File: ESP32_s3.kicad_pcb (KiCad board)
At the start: 2 copper layers, 100 x 80 mm, 67 parts, among them J1 54-00127, J11 backup, J14 TXRX, J15 TXRX2, J3 Conn_01x02, J4 Servo motor, J6 jetson nano, J7 Conn_01x02, J8 Conn_01x02, J9 Conn_01x02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

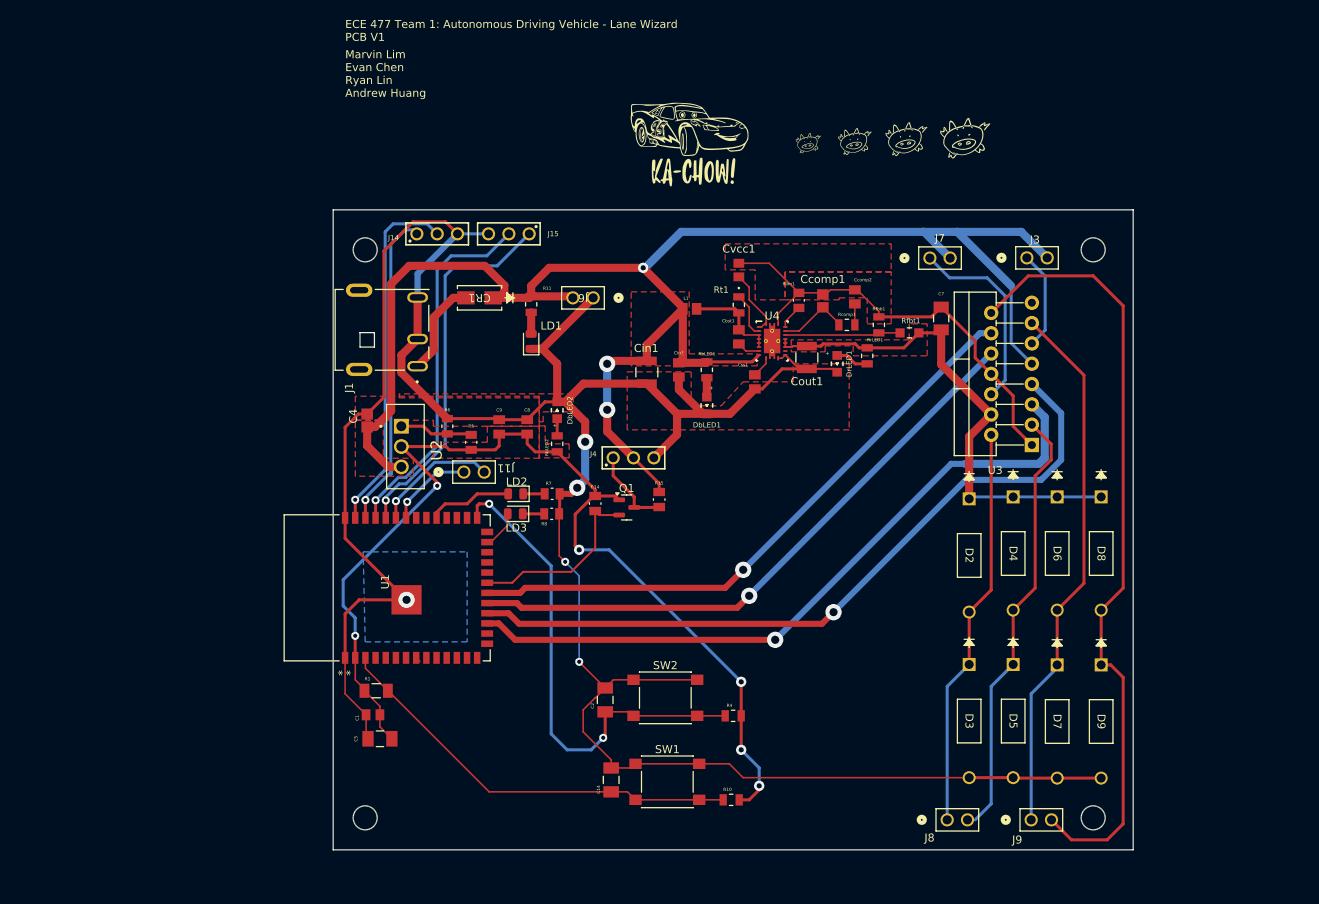
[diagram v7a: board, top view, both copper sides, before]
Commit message: update layout & mounting holes
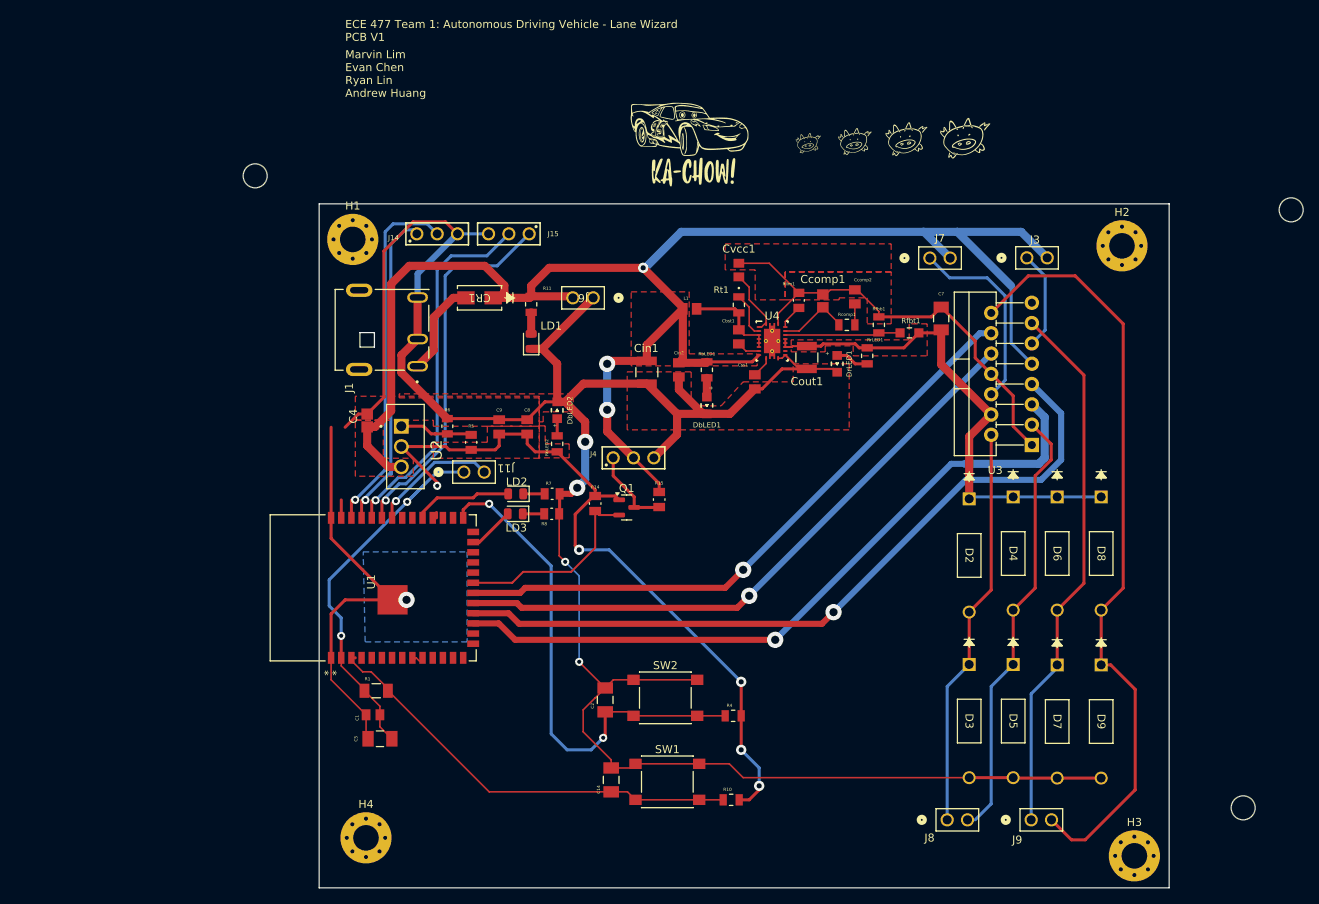
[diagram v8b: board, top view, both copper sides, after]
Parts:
- added H1: MountingHole_Pad, MountingHole:MountingHole_3.2mm_M3_Pad_Via, F.Cu at (107.4, 55.7)
- added H2: MountingHole_Pad, MountingHole:MountingHole_3.2mm_M3_Pad_Via, F.Cu at (203.6, 56.5)
- added H3: MountingHole_Pad, MountingHole:MountingHole_3.2mm_M3_Pad_Via, F.Cu at (205.2, 132.8)
- added H4: MountingHole_Pad, MountingHole:MountingHole_3.2mm_M3_Pad_Via, F.Cu at (109.1, 130.5)
- moved U1 1.75 mm to (110.0, 99.2)
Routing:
- net GPIO9: track 87.3 -> 89.1 mm
- net GPIO13: track 23.1 -> 24.9 mm
- net GPIO12: track 76.5 -> 78.2 mm
- net GPIO11: track 76.4 -> 78.2 mm
- net GPIO10: track 91.8 -> 93.5 mm
- net Net-(D8-A): track 98.5 -> 96.8 mm
- net /GPIO0: track 61.6 -> 63.0 mm
- net /EN: track 52.8 -> 54.2 mm
- net /GPIO38: track 10.6 -> 11.7 mm
- net /GPIO48: track 4.87 -> 5.78 mm
- net GND: track 392.8 -> 393.5 mm
- net 3.3V: track 132.1 -> 132.8 mm
- net /GPIO37: track 0.00 -> 0.67 mm
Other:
- board size 100 x 80 mm -> 132.5 x 90.5 mm
